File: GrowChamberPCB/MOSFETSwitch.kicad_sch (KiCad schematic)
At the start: 5 parts, among them Q1 AO3400A_C347475, Q15 NPN, U17 1N4007W

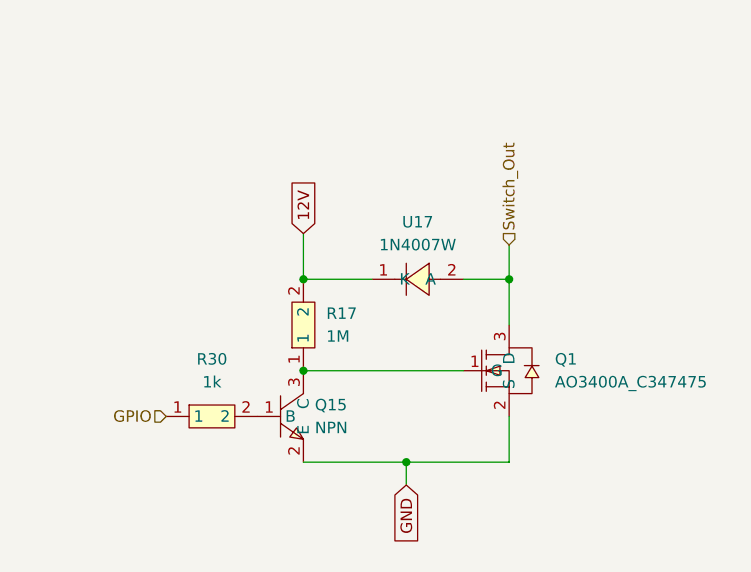
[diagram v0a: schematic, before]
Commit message: Removed 3.3V, wired some stuff
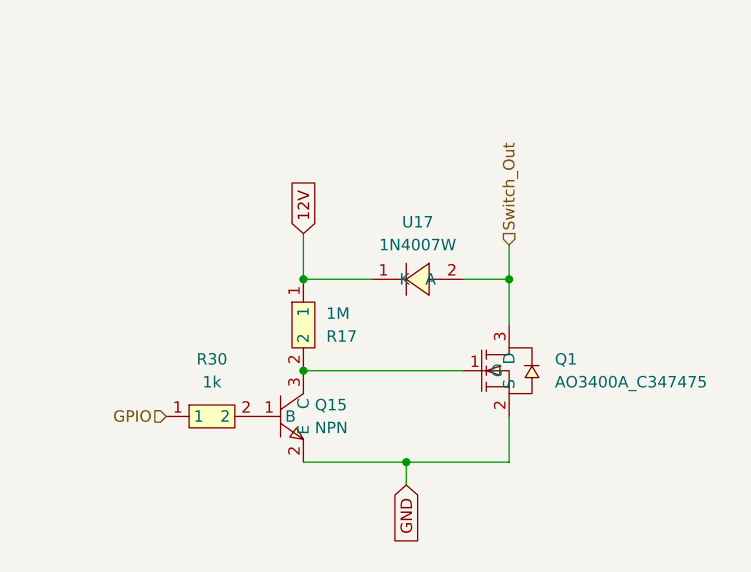
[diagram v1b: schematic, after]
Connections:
- net 12V: now also R17.1; no longer R17.2
- net at Q1.1 (G), Q15.3 (C): now also R17.2; no longer R17.1

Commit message: failing to route the board
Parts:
- added J22, J28, J34: TP, TestPoint:TestPoint_Pad_D2.0mm, symbol Connector_Generic:Conn_01x01
- Q1: value AO3400A_C347475 -> MOSFET
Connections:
- net GPIO: now also J34.1 (Pin_1)
- net Switch_Out: now also J22.1 (Pin_1)
- net at Q1.1 (G), Q15.3 (C), R17.2: now also J28.1 (Pin_1)

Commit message: redesign 3
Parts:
- removed J34: TP, TestPoint:TestPoint_Pad_D2.0mm, symbol Connector_Generic:Conn_01x01
- removed Q1: MOSFET, easyeda2kicad:SOT-23-3_L2.9-W1.3-P1.90-LS2.4-BR, symbol easyeda2kicad:AO3400A_C347475
- removed Q15: NPN, easyeda2kicad:SOT-23-3_L3.0-W1.7-P0.95-LS2.9-BR, symbol easyeda2kicad:2N22221P-TD
- removed R17: 1M, easyeda2kicad:R0603, symbol easyeda2kicad:FRC0603F1004TS
- removed R30: 1k, easyeda2kicad:R0603, symbol easyeda2kicad:FRC0603J102TS
- added Q1: AO3400A, easyeda2kicad:SOT-23-3_L2.9-W1.3-P1.90-LS2.4-BR, symbol easyeda2kicad:AO3400A
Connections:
- net GND: now also Q1.2 (S)
- net Switch_Out: now also Q1.3 (D)
- net 12V: no longer names the net of U17.1 (K)
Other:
- note added: "Basic"
- moved on the sheet: J22

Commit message: finished routing
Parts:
- removed J22, J28: TP, TestPoint:TestPoint_Pad_D2.0mm, symbol Connector_Generic:Conn_01x01
- removed Q1: AO3400A, easyeda2kicad:SOT-23-3_L2.9-W1.3-P1.90-LS2.4-BR, symbol easyeda2kicad:AO3400A
- removed U17: 1N4007W, easyeda2kicad:SOD-123FL_L2.7-W1.8-LS3.7-RD, symbol easyeda2kicad:1N4007W_C7528871
- added D27: 1n4007W, easyeda2kicad:SOD-123FL_L2.7-W1.8-LS3.8-RD, symbol easyeda2kicad:1N4007W_C18199088
- added J34, J35: TP, TestPoint:TestPoint_Pad_D2.0mm, symbol Connector_Generic:Conn_01x01
- added Q7: AO3400A, easyeda2kicad:SOT-23-3_L2.9-W1.3-P1.90-LS2.4-BR, symbol easyeda2kicad:AO3400A
- added R60: 1k, easyeda2kicad:R0603, symbol easyeda2kicad:0603WAF1001T5E
- added R61: 10k, easyeda2kicad:R0603, symbol easyeda2kicad:0603WAF1002T5E
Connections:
- net GND: now also Q7.2 (S), R61.1
- net GPIO: now also R60.1
- net Switch_Out: now also D27.2 (A), J35.1 (Pin_1), Q7.3 (D)
- new net: J34.1 (Pin_1), Q7.1 (G), R60.2, R61.2
- new net 12V: D27.1 (K)
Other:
- note removed: "Basic"

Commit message: started box
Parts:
- removed R61: 10k, easyeda2kicad:R0603, symbol easyeda2kicad:0603WAF1002T5E
- added R40: 10K, easyeda2kicad:R0805, symbol easyeda2kicad:0805W8F1002T5E
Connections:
- net GND: now also R40.1
- net at J34.1 (Pin_1), Q7.1 (G), R60.2: now also R40.2
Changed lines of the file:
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@@
+	(wire
+		(pts
+			(xy 123.19 93.98) (xy 127 93.98)
+		)
+		(stroke
+			(width 0)
+			(type default)
+		)
+	)
+	(wire
+		(pts
+			(xy 134.62 104.14) (xy 134.62 99.06)
+		)
+		(stroke
+			(width 0)
+			(type default)
+		)
+	)
+	(wire
+		(pts
+			(xy 120.65 104.14) (xy 120.65 106.68)
+		)
+		(stroke
+			(width 0)
+			(type default)
+		)
+	)
+	(wire
+		(pts
+			(xy 120.65 93.98) (xy 123.19 93.98)
+		)
+		(stroke
+			(width 0)
+			(type default)
+		)
+	)
+	(wire
+		(pts
+			(xy 120.65 85.09) (xy 124.46 85.09)
+		)
+		(stroke
+			(width 0)
+			(type default)
+		)
+	)
+	(wire
+		(pts
+			(xy 134.62 74.93) (xy 134.62 85.09)
+		)
+		(stroke
+			(width 0)
+			(type default)
+		)
+	)
 	(wire
 		(pts
 			(xy 118.11 93.98) (xy 120.65 93.98)
-		)
-		(stroke
-			(width 0)
-			(type default)
-		)
-	)
-	(wire
-		(pts
-			(xy 123.19 93.98) (xy 127 93.98)
-		)
-		(stroke
-			(width 0)
-			(type default)
-		)
-	)
-	(wire
-		(pts
-			(xy 134.62 104.14) (xy 134.62 99.06)
-		)
-		(stroke
-			(width 0)
-			(type default)
-		)
-	)
-	(wire
-		(pts
-			(xy 120.65 104.14) (xy 120.65 106.68)
-		)
-		(stroke
-			(width 0)
-			(type default)
-		)
-	)
-	(wire
-		(pts
-			(xy 120.65 85.09) (xy 124.46 85.09)
-		)
-		(stroke
-			(width 0)
-			(type default)
-		)
-	)
-	(wire
-		(pts
-			(xy 134.62 74.93) (xy 134.62 85.09)
-		)
-		(stroke
-			(width 0)
-			(type default)
-		)
-	)
-	(wire
-		(pts
-			(xy 120.65 93.98) (xy 123.19 93.98)
 		)
 		(stroke
@@
 	)
 	(symbol
-		(lib_id "easyeda2kicad:0603WAF1002T5E")
-		(at 120.65 99.06 90)
-		(unit 1)
-		(body_style 1)
-		(exclude_from_sim no)
-		(in_bom yes)
-		(on_board yes)
-		(in_pos_files yes)
-		(dnp no)
-		(property "Reference" "R61"
-			(at 116.332 98.552 0)
-			(show_name no)
-			(do_not_autoplace no)
-			(effects
-				(font
-					(size 1.27 1.27)
-				)
-			)
-		)
-		(property "Value" "10k"
-			(at 118.11 98.806 0)
-			(show_name no)
-			(do_not_autoplace no)
-			(effects
-				(font
-					(size 1.27 1.27)
-				)
-			)
-		)
-		(property "Footprint" "easyeda2kicad:R0603"
-			(at 128.27 99.06 0)
-			(hide yes)
-			(show_name no)
-			(do_not_autoplace no)
-			(effects
-				(font
-					(size 1.27 1.27)
-				)
-			)
-		)
-		(property "Datasheet" "https://lcsc.com/product-detail/Chip-Resistor-Surface-Mount-UniOhm_10KR-1002-1_C25804.html"
-			(at 130.81 99.06 0)
-			(hide yes)
-			(show_name no)
-			(do_not_autoplace no)
-			(effects
-				(font
-					(size 1.27 1.27)
-				)
-			)
-		)
-		(property "Description" "10KΩ (1002) ±1%"
-			(at 120.65 99.06 0)
-			(hide yes)
-			(show_name no)
-			(do_not_autoplace no)
-			(effects
-				(font
-					(size 1.27 1.27)
-				)
-			)
-		)
-		(property "Manufacturer" "UNI-ROYAL(厚声)"
-			(at 133.35 99.06 0)
-			(hide yes)
-			(show_name no)
-			(do_not_autoplace no)
-			(effects
-				(font
-					(size 1.27 1.27)
-				)
-			)
-		)
-		(property "MPN" "0603WAF1002T5E"
-			(at 135.89 99.06 0)
-			(hide yes)
-			(show_name no)
-			(do_not_autoplace no)
-			(effects
-				(font
-					(size 1.27 1.27)
-				)
-			)
-		)
-		(property "LCSC Part" "C25804"
-			(at 138.43 99.06 0)
-			(hide yes)
-			(show_name no)
-			(do_not_autoplace no)
-			(effects
-				(font
-					(size 1.27 1.27)
-				)
-			)
-		)
-		(pin "2"
-		)
-		(pin "1"
-		)
-		(instances
-			(project "GrowChamberPCB"
-				(path "/e884bae1-e2d9-44d2-8169-161aa31a84ae/0d345d9a-4cbe-4d19-9fb4-26a36a105e36/03e4cf19-7b8c-4294-9dc9-fc2c3c219f4c"
-					(reference "R69")
-					(unit 1)
-				)
-				(path "/e884bae1-e2d9-44d2-8169-161aa31a84ae/0d345d9a-4cbe-4d19-9fb4-26a36a105e36/16ae4d16-103d-4315-a95d-30ef516bd2be"
-					(reference "R71")
-					(unit 1)
-				)
-				(path "/e884bae1-e2d9-44d2-8169-161aa31a84ae/0d345d9a-4cbe-4d19-9fb4-26a36a105e36/3eb7ef97-2be6-44fc-b442-196b4b54c44d"
-					(reference "R75")
-					(unit 1)
-				)
-				(path "/e884bae1-e2d9-44d2-8169-161aa31a84ae/0d345d9a-4cbe-4d19-9fb4-26a36a105e36/aa2557c2-3763-4fdc-bfc3-8e5913c0b2f6"
-					(reference "R73")
-					(unit 1)
-				)
-				(path "/e884bae1-e2d9-44d2-8169-161aa31a84ae/0d345d9a-4cbe-4d19-9fb4-26a36a105e36/c05d4b5a-fe0c-4974-bc6c-b89e995b6fd8"
-					(reference "R61")
-					(unit 1)
-				)
-				(path "/e884bae1-e2d9-44d2-8169-161aa31a84ae/0d345d9a-4cbe-4d19-9fb4-26a36a105e36/d73ebc8e-acc8-4bb8-89c0-a57dd32680b7"
-					(reference "R67")
-					(unit 1)
-				)
-				(path "/e884bae1-e2d9-44d2-8169-161aa31a84ae/0d345d9a-4cbe-4d19-9fb4-26a36a105e36/e2f79cce-564d-4850-9564-7fa5455408bc"
-					(reference "R65")
-					(unit 1)
-				)
-				(path "/e884bae1-e2d9-44d2-8169-161aa31a84ae/0d345d9a-4cbe-4d19-9fb4-26a36a105e36/e58bfa75-8678-4818-84fb-8fc2b4bb841e"
-					(reference "R63")
-					(unit 1)
-				)
-			)
-		)
-	)
-	(symbol
 		(lib_id "Connector_Generic:Conn_01x01")
 		(at 123.19 88.9 90)
@@
 					(unit 1)
 				)
+			)
+		)
+	)
+	(symbol
+		(lib_id "easyeda2kicad:0805W8F1002T5E")
+		(at 120.65 99.06 90)
+		(unit 1)
+		(body_style 1)
+		(exclude_from_sim no)
+		(in_bom yes)
+		(on_board yes)
+		(in_pos_files yes)
+		(dnp no)
+		(fields_autoplaced yes)
+		(property "Reference" "R40"
+			(at 123.19 97.7899 90)
+			(show_name no)
+			(do_not_autoplace no)
+			(effects
+				(font
+					(size 1.27 1.27)
+				)
+				(justify right)
+			)
+		)
+		(property "Value" "10K"
+			(at 123.19 100.3299 90)
+			(show_name no)
+			(do_not_autoplace no)
+			(effects
+				(font
+					(size 1.27 1.27)
+				)
+				(justify right)
+			)
+		)
+		(property "Footprint" "easyeda2kicad:R0805"
+			(at 128.27 99.06 0)
+			(hide yes)
+			(show_name no)
+			(do_not_autoplace no)
+			(effects
+				(font
+					(size 1.27 1.27)
+				)
+			)
+		)
+		(property "Datasheet" "https://lcsc.com/product-detail/Chip-Resistor-Surface-Mount-UniOhm_10KR-1002-1_C17414.html"
+			(at 130.81 99.06 0)
+			(hide yes)
+			(show_name no)
+			(do_not_autoplace no)
+			(effects
+				(font
+					(size 1.27 1.27)
+				)
+			)
+		)
+		(property "Description" "10KΩ (1002) ±1%"
+			(at 120.65 99.06 0)
+			(hide yes)
+			(show_name no)
+			(do_not_autoplace no)
+			(effects
+				(font
+					(size 1.27 1.27)
+				)
+			)
+		)
+		(property "Manufacturer" "UNI-ROYAL(厚声)"
+			(at 133.35 99.06 0)
+			(hide yes)
+			(show_name no)
+			(do_not_autoplace no)
+			(effects
+				(font
+					(size 1.27 1.27)
+				)
+			)
+		)
+		(property "MPN" "0805W8F1002T5E"
+			(at 135.89 99.06 0)
+			(hide yes)
+			(show_name no)
+			(do_not_autoplace no)
+			(effects
+				(font
+					(size 1.27 1.27)
+				)
+			)
+		)
+		(property "LCSC Part" "C17414"
+			(at 138.43 99.06 0)
+			(hide yes)
+			(show_name no)
+			(do_not_autoplace no)
+			(effects
+				(font
+					(size 1.27 1.27)
+				)
+			)
+		)
+		(pin "2"
+		)
+		(pin "1"
+		)
+		(instances
+			(project "GrowChamberPCB"
+				(path "/e884bae1-e2d9-44d2-8169-161aa31a84ae/0d345d9a-4cbe-4d19-9fb4-26a36a105e36/03e4cf19-7b8c-4294-9dc9-fc2c3c219f4c"
+					(reference "R48")
+					(unit 1)
+				)
+				(path "/e884bae1-e2d9-44d2-8169-161aa31a84ae/0d345d9a-4cbe-4d19-9fb4-26a36a105e36/16ae4d16-103d-4315-a95d-30ef516bd2be"
+					(reference "R49")
+					(unit 1)
+				)
+				(path "/e884bae1-e2d9-44d2-8169-161aa31a84ae/0d345d9a-4cbe-4d19-9fb4-26a36a105e36/3eb7ef97-2be6-44fc-b442-196b4b54c44d"
+					(reference "R51")
+					(unit 1)
+				)
+				(path "/e884bae1-e2d9-44d2-8169-161aa31a84ae/0d345d9a-4cbe-4d19-9fb4-26a36a105e36/aa2557c2-3763-4fdc-bfc3-8e5913c0b2f6"
+					(reference "R50")
+					(unit 1)
+				)
+				(path "/e884bae1-e2d9-44d2-8169-161aa31a84ae/0d345d9a-4cbe-4d19-9fb4-26a36a105e36/c05d4b5a-fe0c-4974-bc6c-b89e995b6fd8"
+					(reference "R40")
+					(unit 1)
+				)
+				(path "/e884bae1-e2d9-44d2-8169-161aa31a84ae/0d345d9a-4cbe-4d19-9fb4-26a36a105e36/d73ebc8e-acc8-4bb8-89c0-a57dd32680b7"
+					(reference "R44")
+					(unit 1)
+				)
+				(path "/e884bae1-e2d9-44d2-8169-161aa31a84ae/0d345d9a-4cbe-4d19-9fb4-26a36a105e36/e2f79cce-564d-4850-9564-7fa5455408bc"
+					(reference "R42")
+					(unit 1)
+				)
+				(path "/e884bae1-e2d9-44d2-8169-161aa31a84ae/0d345d9a-4cbe-4d19-9fb4-26a36a105e36/e58bfa75-8678-4818-84fb-8fc2b4bb841e"
+					(reference "R41")
+					(unit 1)
+				)
